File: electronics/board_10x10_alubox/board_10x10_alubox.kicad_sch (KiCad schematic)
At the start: 26 parts, among them J1 Proto, J10 module_2x15_right_input, J11 module_2x15_right_input, J12 module_2x15_right_input, J2 Proto, J3 Proto, J4 Proto, J5 module_2x15_left_output, J6 module_2x15_left_input, J7 module_2x15_left_input, J8 module_2x15_left_input, J9 module_2x15_right_output

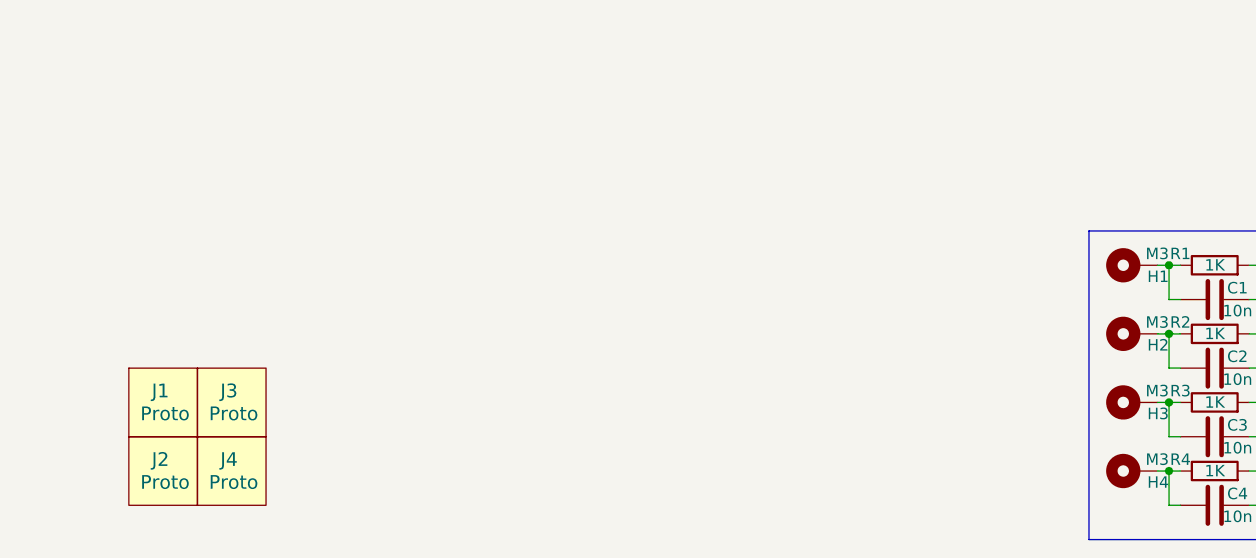
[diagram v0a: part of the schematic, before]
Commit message: WIP adding front LED and power switches
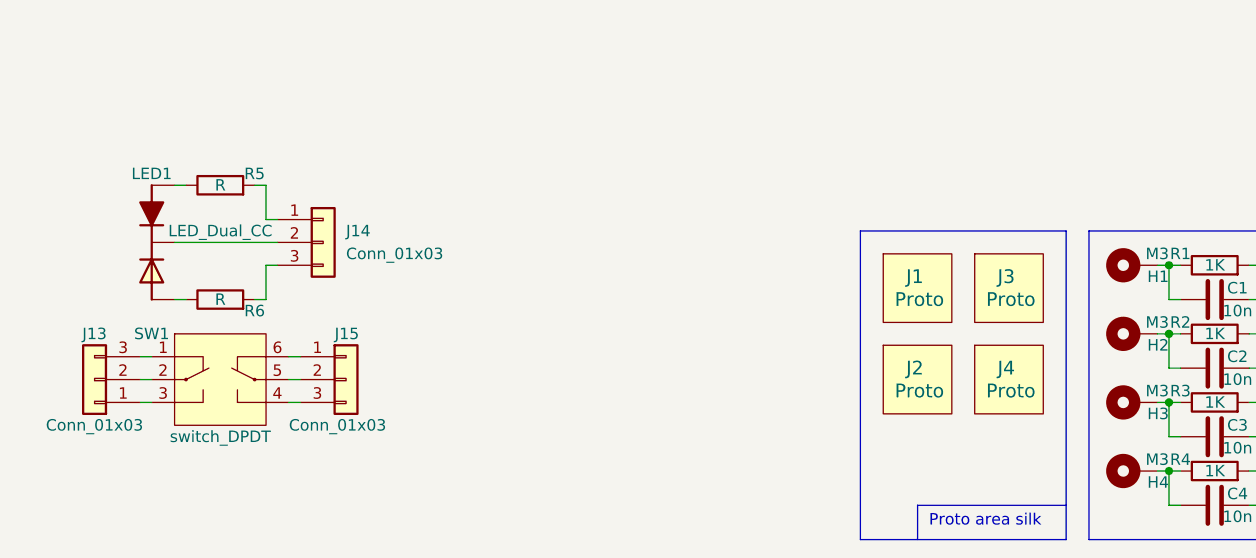
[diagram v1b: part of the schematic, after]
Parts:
- added J13, J14, J15: Conn_01x03, Connector_JST:JST_XA_S03B-XASK-1N-BN_1x03_P2.50mm_Horizontal, symbol Connector_Generic:Conn_01x03
- added LED1: LED_Dual_CC, SquantorDiodes:LED_DUAL_TH245_90deg, symbol SquantorDevice:LED_Dual_CC
- added R5, R6: R, SquantorRcl:R_0603_hand, symbol Device:R
- added SW1: switch_DPDT, symbol SquantorSwitches:switch_DPDT
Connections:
- new net: J13.3 (Pin_3), SW1.1 (SW1_P1)
- new net: J13.2 (Pin_2), SW1.2 (SW1_C1)
- new net: J13.1 (Pin_1), SW1.3 (SW1_P2)
- new net: J15.3 (Pin_3), SW1.4 (SW2_P2)
- new net: J15.2 (Pin_2), SW1.5 (SW2_C1)
- new net: J15.1 (Pin_1), SW1.6 (SW2_P2)
- new net: J14.1 (Pin_1), R5.2
- new net: J14.2 (Pin_2), LED1.2 (C)
- new net: J14.3 (Pin_3), R6.2
- new net: LED1.1 (A1), R5.1
- new net: LED1.3 (A2), R6.1
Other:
- note added: "Proto area silk"
- moved on the sheet: J1, J2, J3, J4

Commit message: further updates and additions to switch and leds
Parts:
- J13, J14, J15: footprint Connector_JST:JST_XA_S03B-XASK-1N-BN_1x03_P2.50mm_Horizontal -> Connector_JST:JST_PH_B3B-PH-K_1x03_P2.00mm_Vertical
- SW1: footprint (none) -> SquantorSwitches:PS-22F02
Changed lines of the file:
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@@
     (property "Reference" "SW1" (id 0) (at 29.21 172.72 0))
     (property "Value" "switch_DPDT" (id 1) (at 36.83 184.15 0))
-    (property "Footprint" "" (id 2) (at 36.83 182.88 0)
+    (property "Footprint" "SquantorSwitches:PS-22F02" (id 2) (at 36.83 182.88 0)
       (effects (font (size 1.27 1.27)) hide)
     )
@@
       (effects (font (size 1.27 1.27)) (justify left))
     )
-    (property "Footprint" "Connector_JST:JST_XA_S03B-XASK-1N-BN_1x03_P2.50mm_Horizontal" (id 2) (at 48.26 162.56 0)
+    (property "Footprint" "Connector_JST:JST_PH_B3B-PH-K_1x03_P2.00mm_Vertical" (id 2) (at 48.26 162.56 0)
       (effects (font (size 1.27 1.27)) hide)
     )
@@
     (property "Reference" "J13" (id 0) (at 22.86 172.72 0))
     (property "Value" "Conn_01x03" (id 1) (at 22.86 182.88 0))
-    (property "Footprint" "Connector_JST:JST_XA_S03B-XASK-1N-BN_1x03_P2.50mm_Horizontal" (id 2) (at 22.86 177.8 0)
+    (property "Footprint" "Connector_JST:JST_PH_B3B-PH-K_1x03_P2.00mm_Vertical" (id 2) (at 22.86 177.8 0)
       (effects (font (size 1.27 1.27)) hide)
     )
@@
       (effects (font (size 1.27 1.27)) (justify left))
     )
-    (property "Footprint" "Connector_JST:JST_XA_S03B-XASK-1N-BN_1x03_P2.50mm_Horizontal" (id 2) (at 50.8 177.8 0)
+    (property "Footprint" "Connector_JST:JST_PH_B3B-PH-K_1x03_P2.00mm_Vertical" (id 2) (at 50.8 177.8 0)
       (effects (font (size 1.27 1.27)) hide)
     )
@@
     )
     (path "/30f9942b-c84a-4715-9728-61397c2814d4"
-      (reference "J13") (unit 1) (value "Conn_01x03") (footprint "Connector_JST:JST_XA_S03B-XASK-1N-BN_1x03_P2.50mm_Horizontal")
+      (reference "J13") (unit 1) (value "Conn_01x03") (footprint "Connector_JST:JST_PH_B3B-PH-K_1x03_P2.00mm_Vertical")
     )
     (path "/301ff6ed-6d4c-44b8-84ea-ea4014e21c96"
-      (reference "J14") (unit 1) (value "Conn_01x03") (footprint "Connector_JST:JST_XA_S03B-XASK-1N-BN_1x03_P2.50mm_Horizontal")
+      (reference "J14") (unit 1) (value "Conn_01x03") (footprint "Connector_JST:JST_PH_B3B-PH-K_1x03_P2.00mm_Vertical")
     )
     (path "/4a0ef56d-d7d7-4f3f-878d-0c94d8538538"
-      (reference "J15") (unit 1) (value "Conn_01x03") (footprint "Connector_JST:JST_XA_S03B-XASK-1N-BN_1x03_P2.50mm_Horizontal")
+      (reference "J15") (unit 1) (value "Conn_01x03") (footprint "Connector_JST:JST_PH_B3B-PH-K_1x03_P2.00mm_Vertical")
     )
     (path "/83a755b7-e349-4644-860f-22658c62358e"
@@
     )
     (path "/0d944d89-291e-4c85-8822-b8e0cb54a1ac"
-      (reference "SW1") (unit 1) (value "switch_DPDT") (footprint "")
-    )
-  )
+      (reference "SW1") (unit 1) (value "switch_DPDT") (footprint "SquantorSwitches:PS-22F02")
+    )
+  )

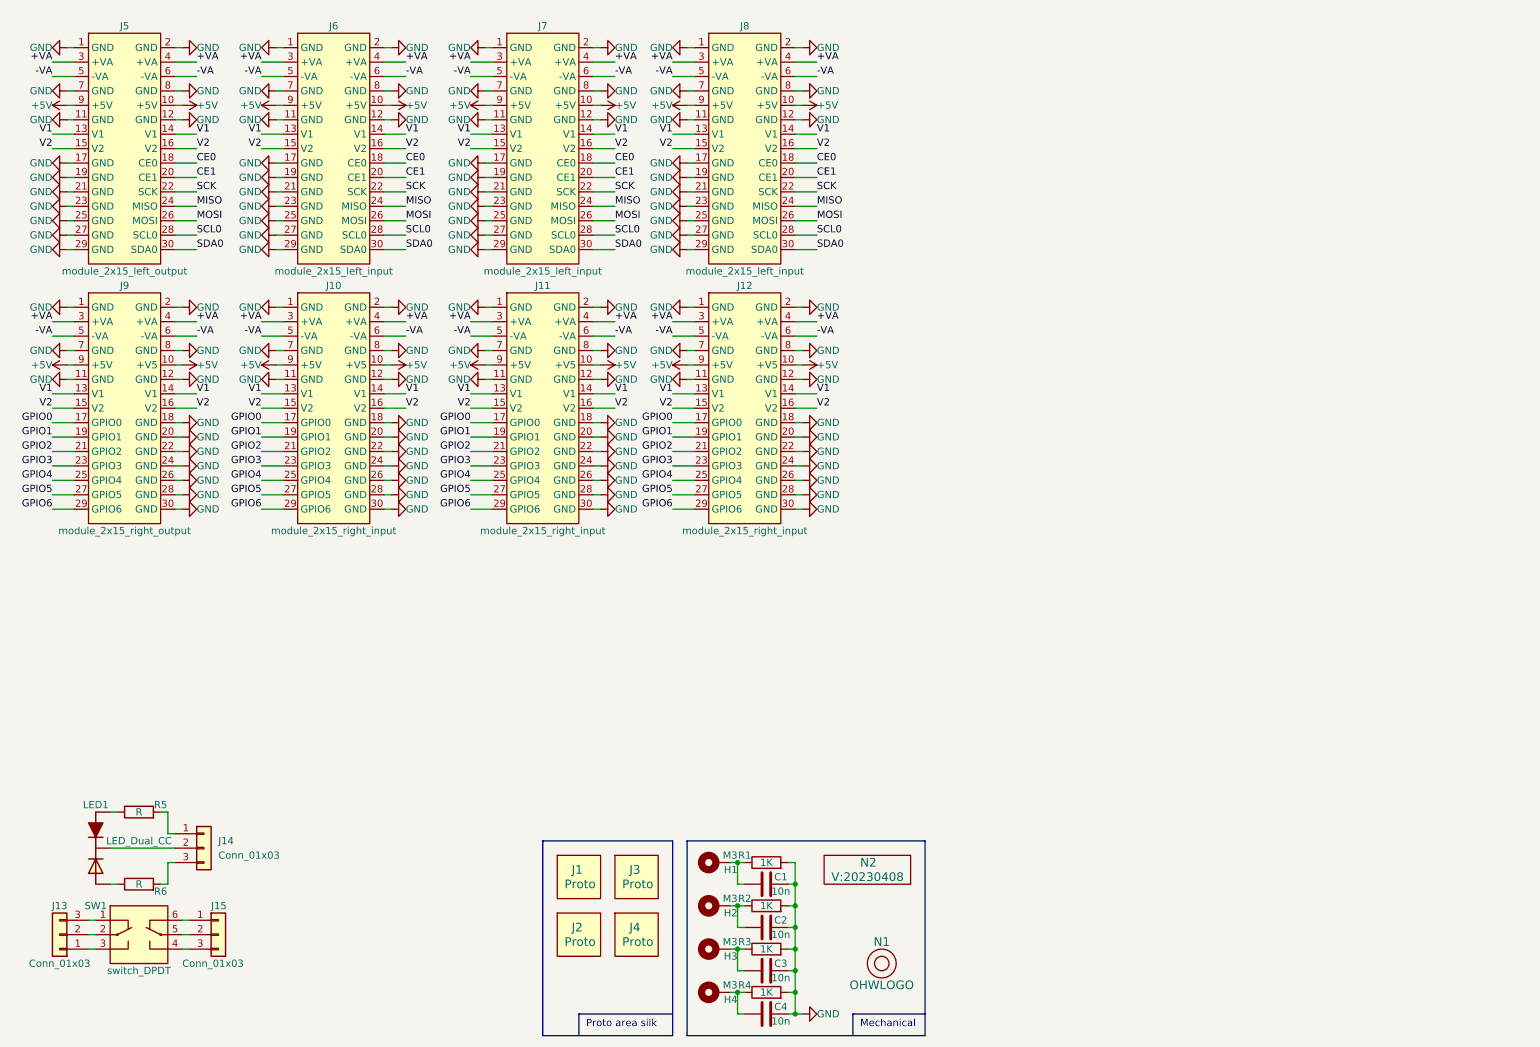
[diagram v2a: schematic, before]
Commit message: added addional leds and routed one corner
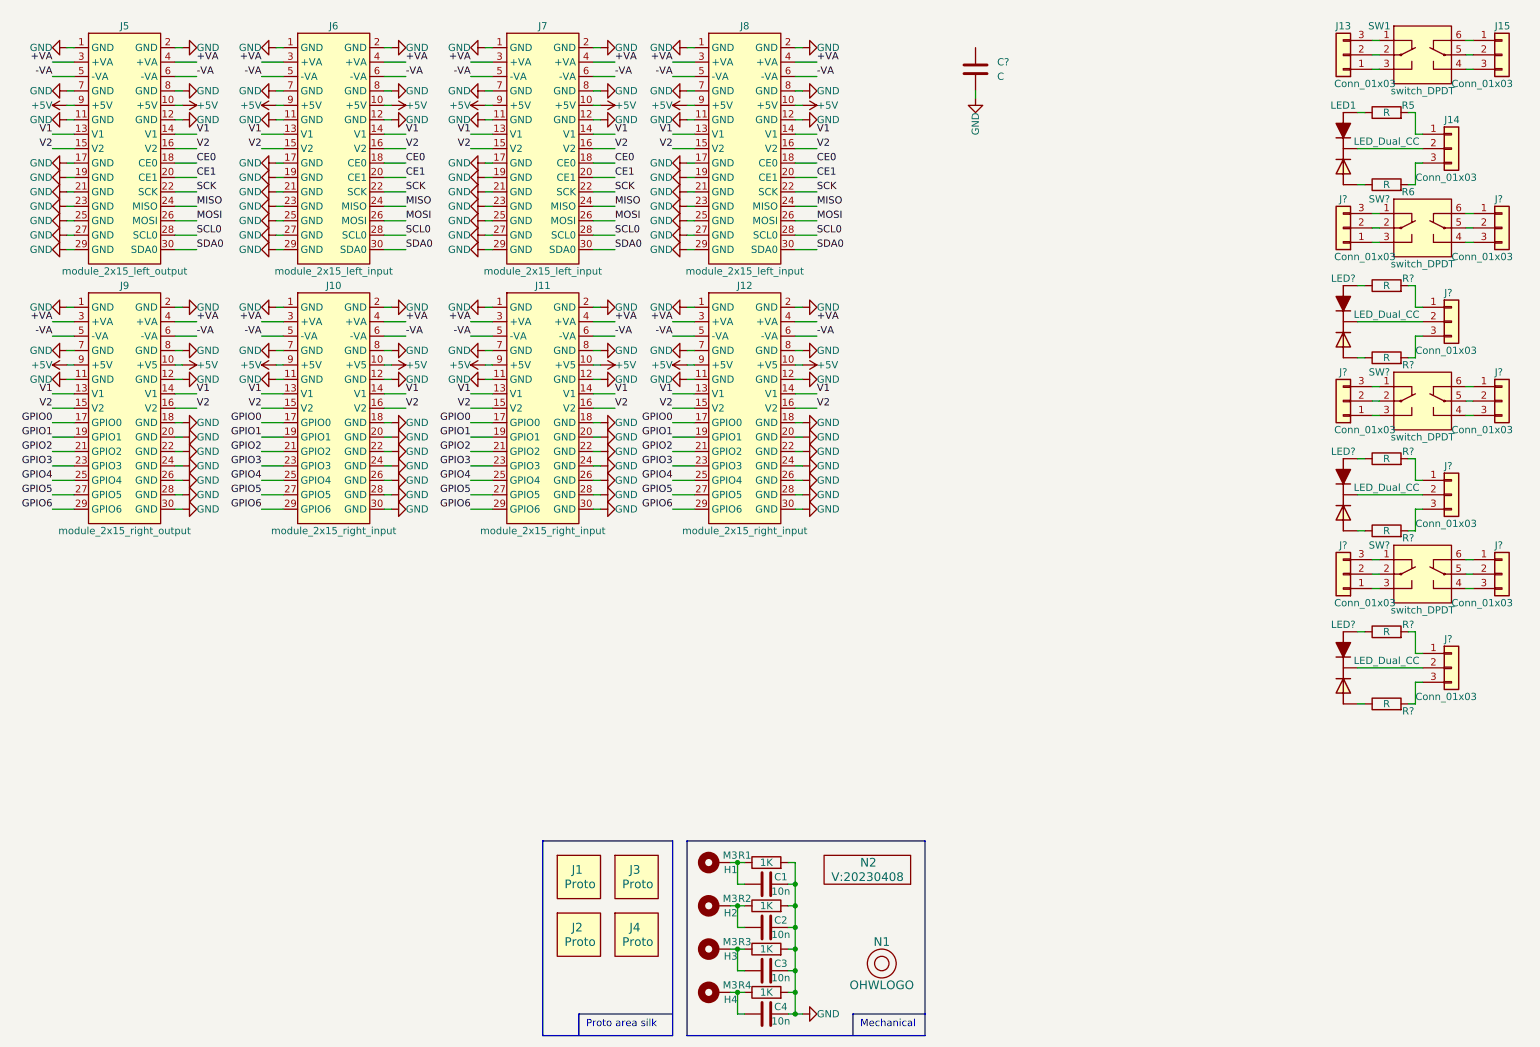
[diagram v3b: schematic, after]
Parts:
- added C?: C, symbol Device:C
- added J? (x9): Conn_01x03, Connector_JST:JST_PH_B3B-PH-K_1x03_P2.00mm_Vertical, symbol Connector_Generic:Conn_01x03
- added LED? (x3): LED_Dual_CC, SquantorDiodes:LED_DUAL_TH245_90deg, symbol SquantorDevice:LED_Dual_CC
- added R? (x6): R, SquantorRcl:R_0603_hand, symbol Device:R
- added SW? (x3): switch_DPDT, SquantorSwitches:PS-22F02, symbol SquantorSwitches:switch_DPDT
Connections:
- net GND: now also C?.2
- new net: LED?.1 (A1), R?.1 (x3)
- new net: J?.2 (Pin_2), LED?.2 (C) (x3)
- new net: LED?.3 (A2), R?.1 (x3)
- new net: J?.1 (Pin_1), SW?.6 (SW2_P2) (x3)
- new net: J?.2 (Pin_2), SW?.5 (SW2_C1) (x3)
- new net: J?.3 (Pin_3), SW?.4 (SW2_P2) (x3)
- new net: J?.3 (Pin_3), SW?.1 (SW1_P1) (x3)
- new net: J?.2 (Pin_2), SW?.2 (SW1_C1) (x3)
- new net: J?.1 (Pin_1), SW?.3 (SW1_P2) (x3)
- new net: J?.3 (Pin_3), R?.2 (x3)
- new net: J?.1 (Pin_1), R?.2 (x3)
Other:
- moved on the sheet: J13, J14, J15, LED1, R5, R6, SW1

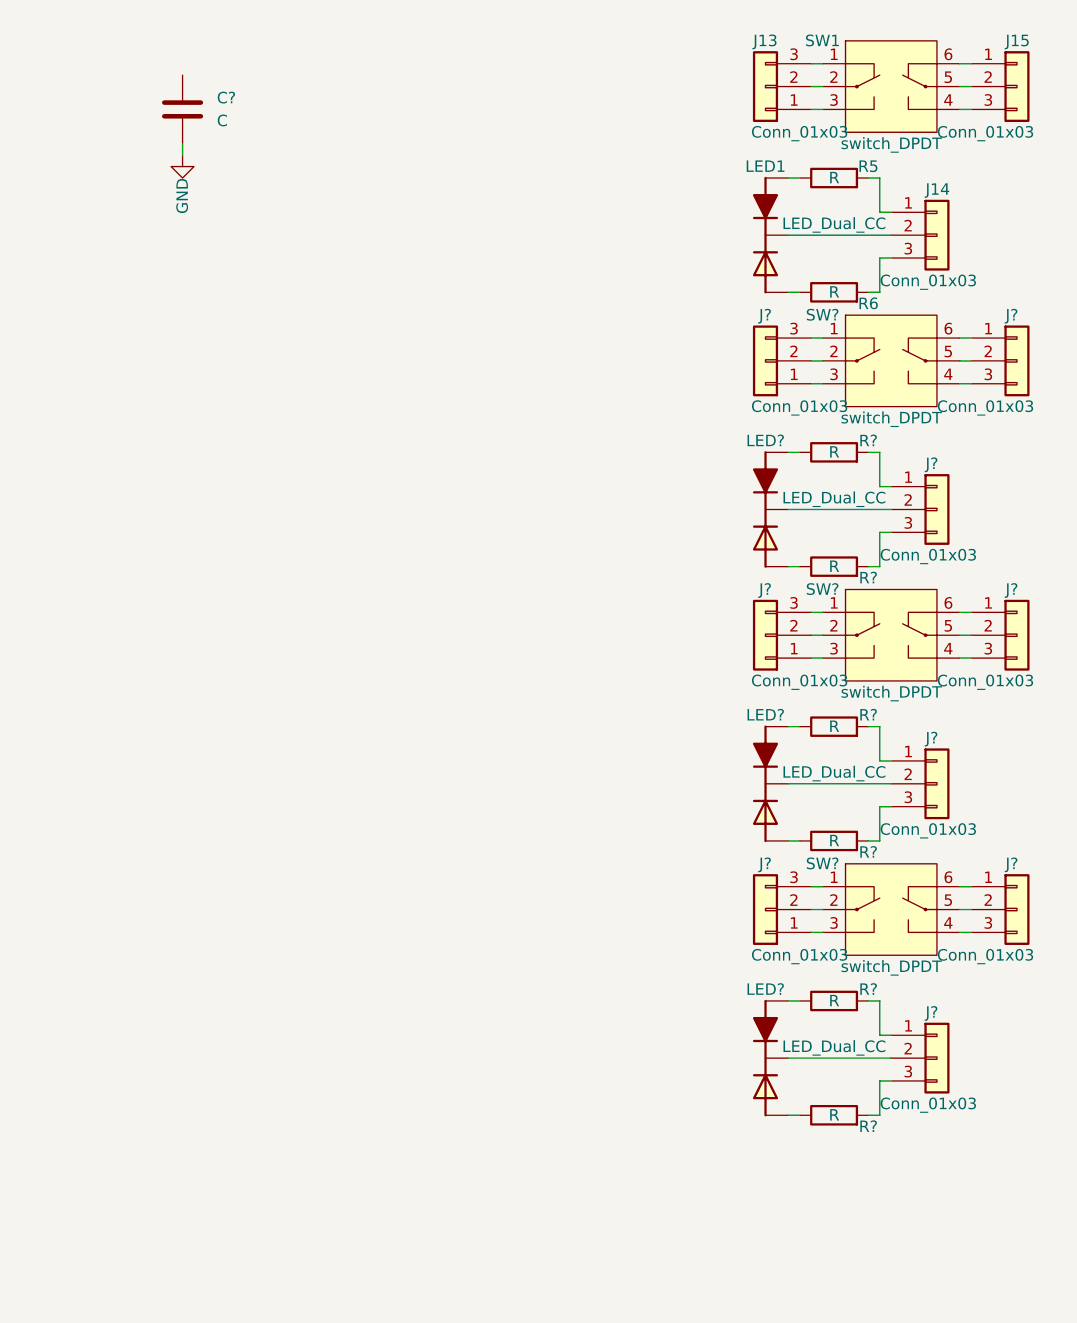
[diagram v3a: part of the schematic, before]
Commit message: place and route LED and switches
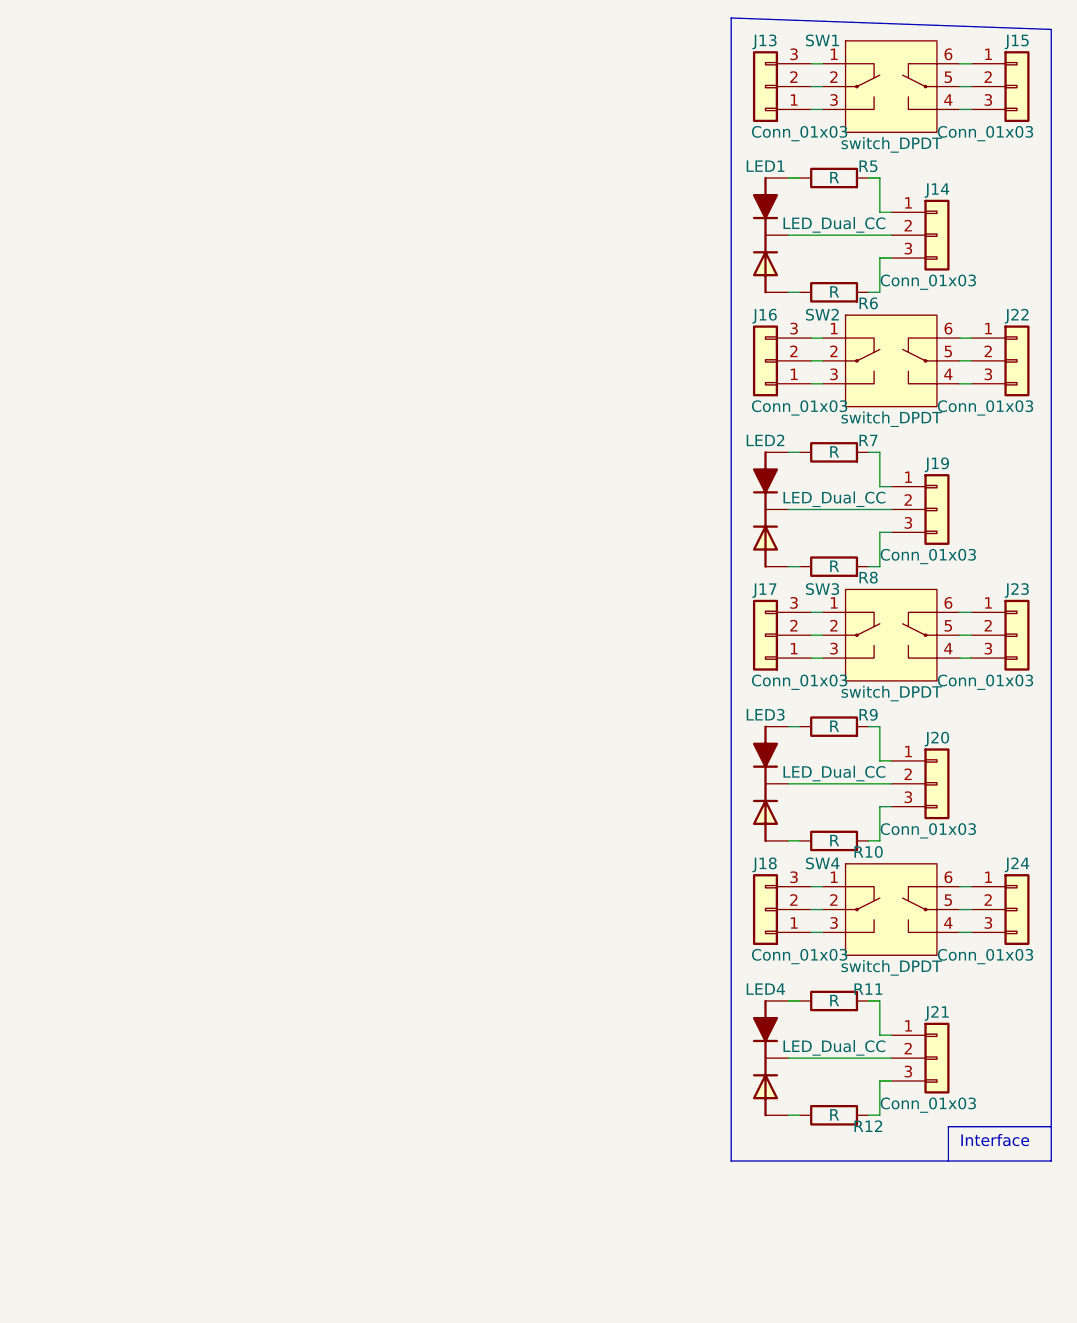
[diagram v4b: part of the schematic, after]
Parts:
- removed C?: C, symbol Device:C
- gave numbers to parts that had none: 21
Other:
- note added: "Interface"
